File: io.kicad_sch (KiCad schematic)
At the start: 56 parts, among them J1 WAFER-MX3.0-12PZZ, Q1 AM2390N-TP, Q2 AM2390N-TP, U4 SIT1051AT/3

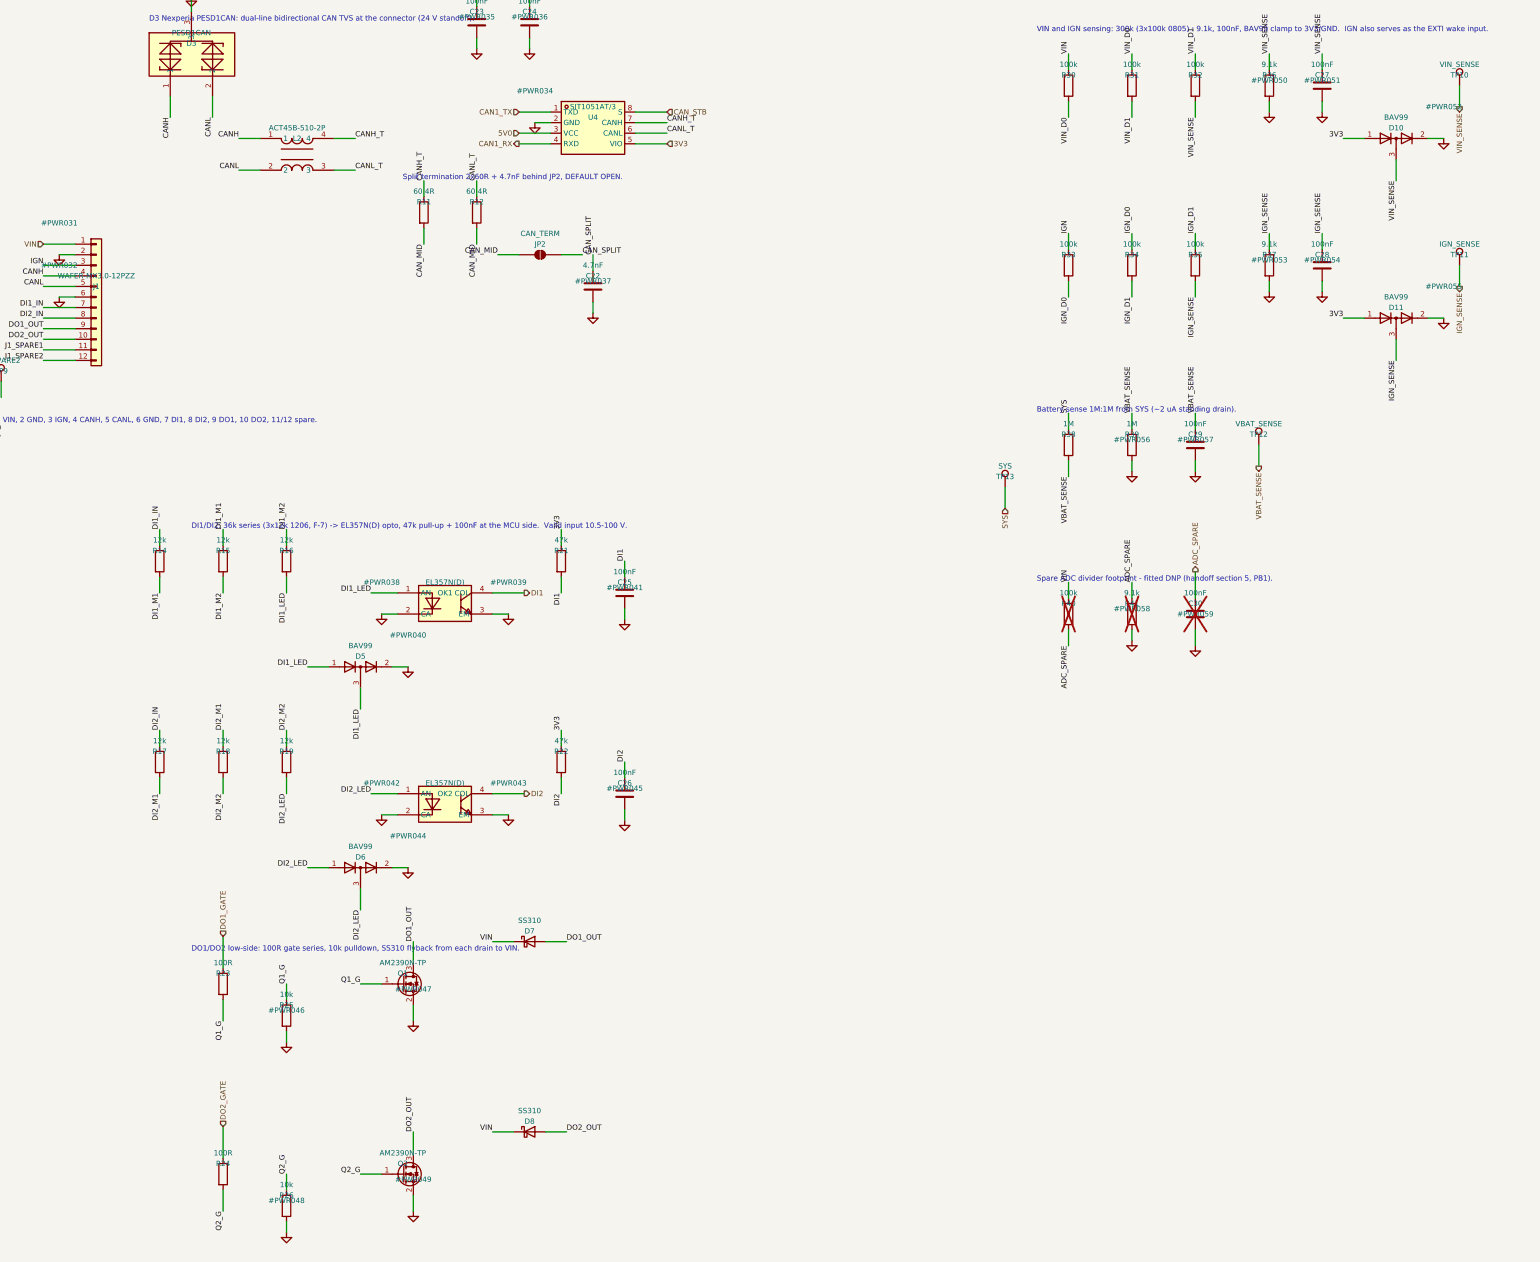
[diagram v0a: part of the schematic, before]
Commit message: M2: io re-committed ERC-clean with F-10 + F-11 applied
F-10: two-stage non-inverting NPN gate driver (2x MMBT3904 C20526 + 4.7k/
10k/10k/2.2k per channel) from 5V0; gate swing ~4.1V where AM2390N RDS is
specified. Default-OFF proven structurally by the netlist guard (8/8
assertions: gate pulldown, MCU-side base pulldown, QnB base pullup, QnB
collector on driver node, both channels). Consequence logged: DO1/DO2
inactive during battery backup. handoff section 6 note updated per
instruction.
F-11: SS310 -> SS3200 C65001 (200V 3A SMA), both channels.
ERC 0 errors; section-5 checklist 48/48 with far ends updated.
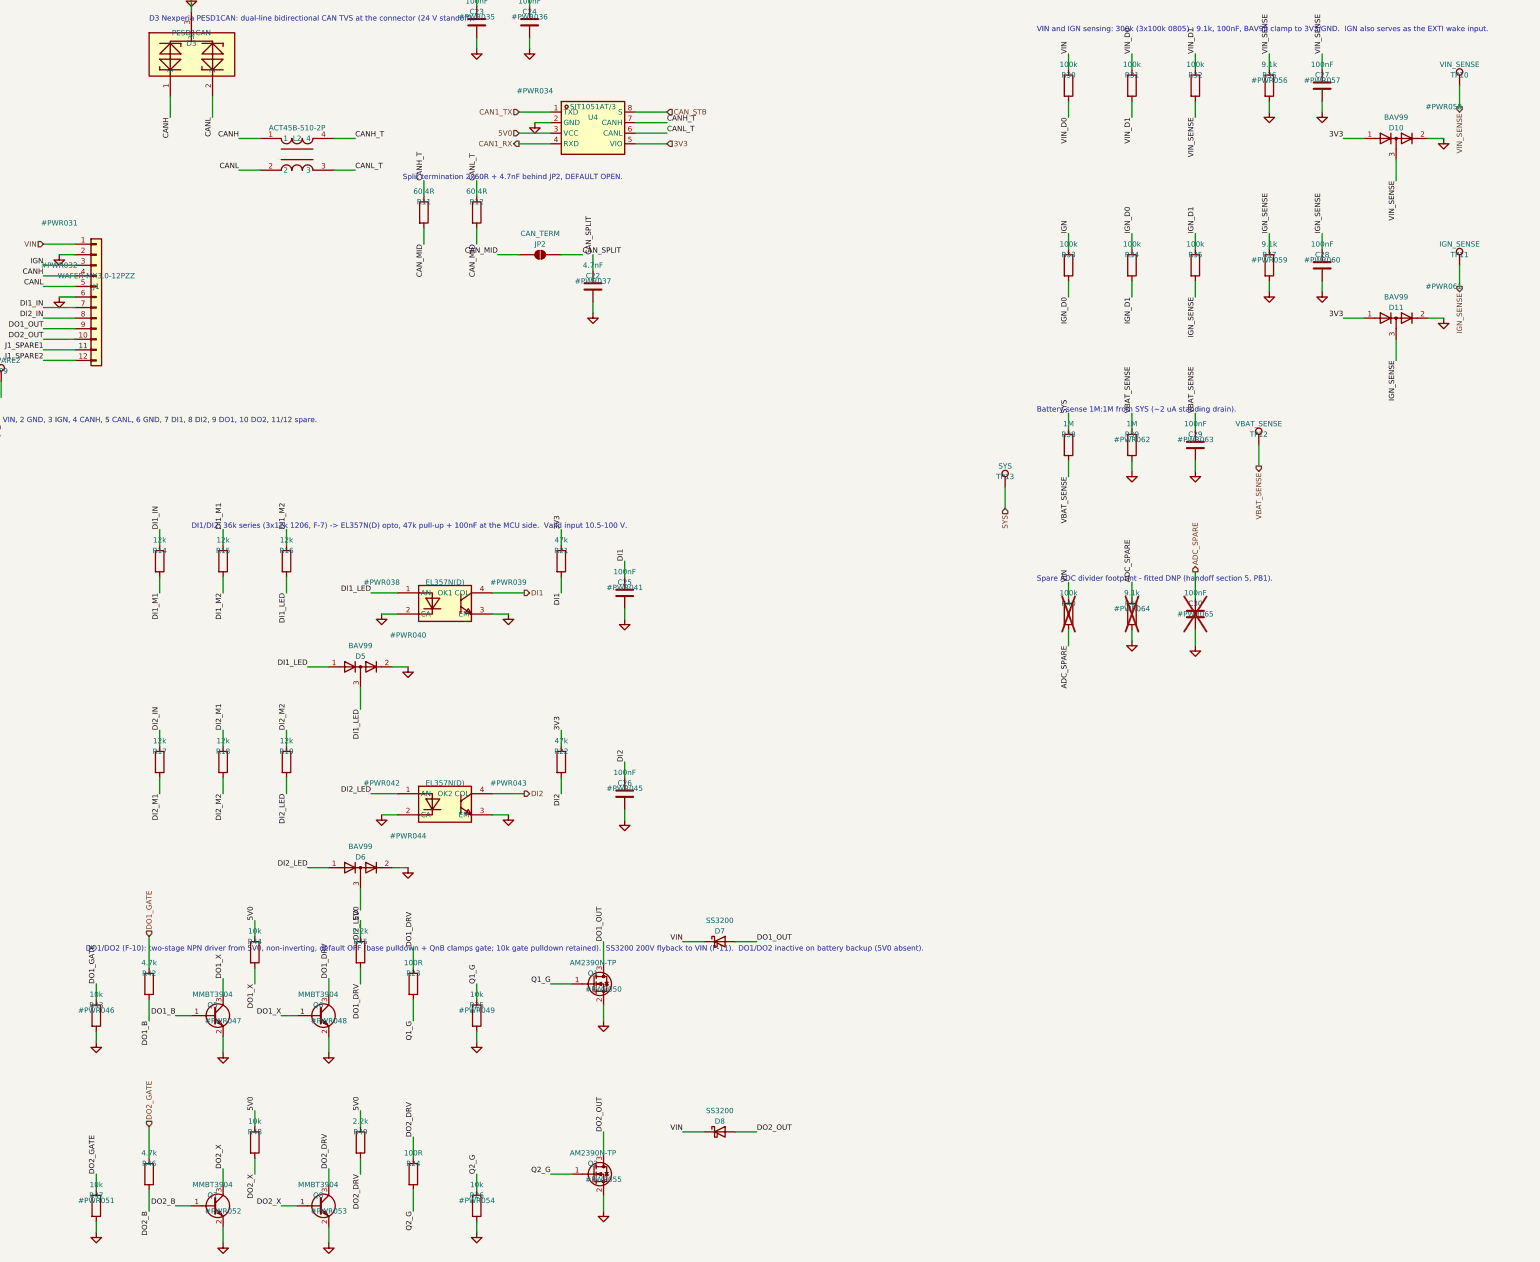
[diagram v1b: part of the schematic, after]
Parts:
- added Q5, Q6, Q7, Q8: MMBT3904, Package_TO_SOT_SMD:SOT-23, symbol Transistor_BJT:Q_NPN_BEC
- added R42, R46: 4.7k, Resistor_SMD:R_0805_2012Metric, symbol Device:R
- added R43, R44, R47, R48: 10k, Resistor_SMD:R_0805_2012Metric, symbol Device:R
- added R45, R49: 2.2k, Resistor_SMD:R_0805_2012Metric, symbol Device:R
- D7, D8: value SS310 -> SS3200; LCSC C15874 -> C65001
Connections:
- net 5V0: now also R44.1, R45.1, R48.1, R49.1
- net DO1_GATE: now also R42.1, R43.1; no longer R23.1
- net DO2_GATE: now also R46.1, R47.1; no longer R24.1
- net GND: now also Q5.2 (E), Q6.2 (E), Q7.2 (E), Q8.2 (E), R43.2, R47.2
- new net DO1_B: Q5.1 (B), R42.2
- new net DO1_DRV: Q6.3 (C), R23.1, R45.2
- new net DO1_X: Q5.3 (C), Q6.1 (B), R44.2
- new net DO2_B: Q7.1 (B), R46.2
- new net DO2_DRV: Q8.3 (C), R24.1, R49.2
- new net DO2_X: Q7.3 (C), Q8.1 (B), R48.2
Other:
- note added: "DO1/DO2 (F-10): two-stage NPN driver from 5V0, non-inverting, default OFF (base pulldown + QnB clamps gate; 10k gate pulldown retained). SS3200 200V flyback to VIN (F-11). DO1/DO2 inactive on battery backup (5V0 absent)."
- note removed: "DO1/DO2 low-side: 100R gate series, 10k pulldown, SS310 flyback from each drain to VIN."
- moved on the sheet: D7, D8, Q1, Q2, R23, R24, R25, R26
